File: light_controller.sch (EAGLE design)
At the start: 96 parts, among them IC1 ULN2803A, U1 DAC5578SPW, U2 LM3480IM3-5.0, U3 RCD-24-0.70

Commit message: updated all elements in schematic to be from openag_eagle_library repo
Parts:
- removed C12: 4.7uF, rcl:C-USC1206
- removed C13: 0.1uF, rcl:C-USC0603
- removed F6: (no value), fuse:GSH15
- removed IC1: ULN2803A, uln-udn:ULN2803A
- removed LED9: (no value), led:LED
- removed R17: 10k, rcl:R-US_R0603
- removed R18, R19, R20, R21, R25, R26, R27, R28: 0 ohm, rcl:R-US_R0603
- removed R24: 10 ohm, rcl:R-US_R0603
- removed R29, R30: 1K, rcl:R-US_R0603
- removed RELAY_1: G5LE-14_DC12, relay_2:G5LE-14_DC12
- removed S1: (no value), switch-omron:10-XX
- removed U$2: PHOTON_WITH_HEADERS, Spark:PHOTON_WITH_HEADERS
- removed U$4: SMAJ14A, openag_diodes:SMAJ14A
- added *CH7+, *CH7-: WIREPAD3,17/1,3, wirepad:WIREPAD3,17/1,3
- added C19, C20: 10uF, openag-capacitors:10UF-CL31B106KBHNNNE
- added D1: SMAJ14A, openag-diodes:SMAJ14A
- added F2, F3: SST 7, openag-fuses:SST_7
- added IC2: ULN2803A, openag-transistors:ULN2803DIP
- added LED2: (no value), openag-diodes:APT1608QBC/DCHIPLED_0603
- added R10, R13, R14, R15, R8, R9: 0 ohm, openag-resistors:0OHM-ERJ-3GEY0R00V
- added R3, R4: 10K, openag-resistors:10K-ERJ-3EKF1002V
- added R5, R6, R7: 1K, openag-resistors:1K-ERJ-PB3D1001V
- added TP26, TP27: PTR1B2,54, testpad:PTR1B2,54
- added U4: G5LE-14 DC24, openag-relays:G5LE-14_DC24
- added U5: ISO1540DR, openag-isolators:ISO1540DR
- C1: value 1uF -> 4.7uF; device rcl:C-USC0603 -> openag-capacitors:4.7UF-C1206C475K5PACTU
- C10, C3, C5: device rcl:C-USC1206 -> openag-capacitors:4.7UF-C1206C475K5PACTU
- C11, C8: value 10uF -> 0.1uF; device rcl:C-USC1206 -> openag-capacitors:0.1UF-C1206C104K5RAC7867
- C2, C6: device rcl:C-USC0603 -> openag-capacitors:0.1UF-C1206C104K5RAC7867
- C4: device rcl:C-USC1206 -> openag-capacitors:10UF-CL31B106KBHNNNE
- C7: value 10uF -> 1uF; device rcl:C-USC1206 -> openag-capacitors:1UF-CL10A105KB8NNNC
- C9: value 0.1uF -> 10uF; device rcl:C-USC0603 -> openag-capacitors:10UF-CL31B106KBHNNNE
- F1: value (none) -> SST 7; device fuse:GSH15 -> openag-fuses:SST_7
- L1: device openag-inductors:74404064121 -> openag-inductors:120UH-74404064121
- LED1: device led:LEDCHIP-LED0603 -> openag-diodes:APT1608QBC/DCHIPLED_0603
- R1: value 10K -> 10 ohm; device rcl:R-US_R0603 -> openag-resistors:10OHM-ERJ-3GEYJ100V
- R11, R12: value 1K -> 0 ohm; device rcl:R-US_R0603 -> openag-resistors:0OHM-ERJ-3GEY0R00V
- R2: value 0 ohm -> 1K; device rcl:R-US_R0603 -> openag-resistors:1K-ERJ-PB3D1001V
- TP1, TP2: device testpad:PTR1B2,54 -> openag-testpoints:PTR1B2,54
- U$1: value PSOC_4000 -> PHOTON_WITH_HEADERS; device stovelite:PSOC_4000 -> openag-microcontrollers:PHOTON_WITH_HEADERS
- U$3: value ISO1540 -> PSOC_4000; device ISO1540:ISO1540 -> openag-microcontrollers:PSOC_4000
- U2: device LEDdynamics:LM3480IM3-5.0 -> openag-regulators:LM3480IM3-5.0
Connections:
- removed net +12V: IC1.CD+, R24.1, RELAY_1.1, RELAY_1.2
- removed net 1C: IC1.O1, RELAY_1.5, TP1.TP
- removed net N$13: LED9.A, R17.1
- removed net N$4: IC1.I1, R2.2
- removed net P0: R17.2, R2.1
- removed net R1: F1.2, R1.2, TP2.TP
- new net CH7-: *CH7-.P, F1.2, R3.2, TP2.TP, TP27.TP
- new net DIM2: U1.VOUT_B
- new net DIM3: U1.VOUT_C
- new net DIM4: U1.VOUT_D
- new net DIM5: U1.VOUT_E
- new net DIM6: U1.VOUT_F
- new net N$5: F3.1, U3.+VOUT
- new net N$7: LED2.A, R4.1
- new net O1: IC2.18, TP1.TP, U4.5
- new net P6: U$3.P1.1
- new net P7: IC2.1, R4.2, U$3.P0.6
- net +24V: now also *CH7+.P, F2.2, IC2.10, R1.1, TP26.TP, U4.1, U4.2; no longer F6.2
- net +3V3: now also C1.1, C20.1, R2.2, R5.2, R8.2, U$3.VDD, U5.VCC2; no longer C3.1, C8.1, R18.2, R29.2, R30.2, S1.S1, U$1.VDD, U$3.VCC2
- net 24V_IN: now also C10.1, C9.1, D1.P$2, F2.1; no longer C12.1, C13.1, F6.1, U$4.P$2
- net CH1+: now also F3.2; no longer U3.+VOUT
- net GND1: now also C19.2, U5.GND1; no longer C7.2, U$3.GND1
- net GND2: now also C20.2, C7.2, D1.P$1, IC2.9, LED2.C, U$1.GND@2, U$1.GND@21, U$3.VSS, U5.GND2; no longer C12.2, C13.2, IC1.GND, LED9.C, U$1.VSS, U$2.GND@2, U$2.GND@21, U$3.GND2, U$4.P$1
- net I2C_3V3: now also C19.1, R6.2, R7.2, U5.VCC1; no longer C7.1, R11.2, R12.2, U$3.VCC1
- net I2C_SCL: now also R6.1, R7.1, U5.SCL1; no longer R12.1, U$3.SCL1
- net I2C_SDA: now also U5.SDA1; no longer R11.1, U$3.SDA1
- net N$1: now also R3.1; no longer R1.1
- net N$2: now also U4.3; no longer RELAY_1.3
- net N$21: now also R13.1, U$1.D2; no longer R26.1, U$2.D2
- net N$22: now also R14.1, U$1.D1; no longer R27.1, U$2.D1
- net N$23: now also C3.1, C8.1, R8.1, U$1.3V3; no longer C10.1, C9.1, R18.1, U$2.3V3
- net N$24: now also R9.1, U$1.D6; no longer R19.1, U$2.D6
- net N$25: now also R10.1, U$1.D5; no longer R20.1, U$2.D5
- net N$26: now also R11.1, U$1.D4; no longer R21.1, U$2.D4
- net N$27: now also R12.1, U$1.D3; no longer R25.1, U$2.D3
- net N$28: now also R15.1, U$1.D0; no longer R28.1, U$2.D0
- net N$29: now also C7.1, U$3.VCCD; no longer C1.1, U$1.VCCD
- net N$39: now also R1.2; no longer R24.2
- net P1: now also R9.2, U$3.P2.0; no longer R19.2, S1.P1, U$1.P2.0
- net P2: now also R10.2, U$3.P1.7; no longer R20.2, U$1.P1.7
- net P3: now also R11.2, U$3.P1.6; no longer R21.2, U$1.P1.6
- net P4: now also R12.2, U$3.P1.3; no longer R25.2, U$1.P1.3
- net P5: now also R13.2, U$3.P1.2; no longer R26.2, U$1.P1.2
- net SCL: now also R14.2, R5.1, U$3.P3.1, U5.SCL2; no longer R27.2, R30.1, U$1.P3.1, U$3.SCL2
- net SDA: now also R15.2, R2.1, U$3.P3.0, U5.SDA2; no longer R28.2, R29.1, U$1.P3.0, U$3.SDA2
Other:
- note added: "Current Regulators Module"
- note added: "Multi-Channel DAC Module"
- note added: "TODO: Same circuit for channels 2-6"
- note removed: "LM3480IM3-5.0"
- note removed: "Pushbutton Switch Module"
- moved on the sheet: C14, C15, C16, C17, C18, C9, L1, LED1, TP1, TP2, U1, U3

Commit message: calculated power consuption, cleaned up mcu 0ohnm resistors
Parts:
- removed *CH7+, *CH7-: WIREPAD3,17/1,3, wirepad:WIREPAD3,17/1,3
- removed C4: 10uF, openag-capacitors:10UF-CL31B106KBHNNNE
- removed C5: 4.7uF, openag-capacitors:4.7UF-C1206C475K5PACTU
- removed C6: 0.1uF, openag-capacitors:0.1UF-C1206C104K5RAC7867
- removed F1: SST 7, openag-fuses:SST_7
- removed IC2: ULN2803A, openag-transistors:ULN2803DIP
- removed LED1, LED2: (no value), openag-diodes:APT1608QBC/DCHIPLED_0603
- removed R1: 10 ohm, openag-resistors:10OHM-ERJ-3GEYJ100V
- removed TP1, TP2: PTR1B2,54, openag-testpoints:PTR1B2,54
- removed TP11, TP26, TP27: PTR1B2,54, testpad:PTR1B2,54
- removed U2: LM3480IM3-5.0, openag-regulators:LM3480IM3-5.0
- removed U4: G5LE-14 DC24, openag-relays:G5LE-14_DC24
- added R16, R17, R18, R20, R21, R22, R23, R24, R25, R26, R27, R28, R29, R30, R31, R32, R33: 0 ohm, openag-resistors:0OHM-ERJ-3GEY0R00V
- C1: value 4.7uF -> 1uF; device openag-capacitors:4.7UF-C1206C475K5PACTU -> openag-capacitors:1UF-CL10A105KB8NNNC
- C7: value 1uF -> 0.1uF; device openag-capacitors:1UF-CL10A105KB8NNNC -> openag-capacitors:0.1UF-C1206C104K5RAC7867
- R3, R4: value 10K -> 0 ohm; device openag-resistors:10K-ERJ-3EKF1002V -> openag-resistors:0OHM-ERJ-3GEY0R00V
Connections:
- removed net CH7-: *CH7-.P, F1.2, R3.2, TP2.TP, TP27.TP
- removed net N$39: C4.1, R1.2, U2.IN
- removed net O1: IC2.18, TP1.TP, U4.5
- new net N$10: R21.1, U$3.P1.7
- new net N$11: R22.1, U$3.P1.6
- new net N$12: R23.1, U$3.P1.3
- new net N$13: R24.1, U$3.P1.2
- new net N$14: R25.1, U$3.P1.1
- new net N$15: C7.2, R26.2
- new net N$16: C1.1, C2.1, R27.1, U$3.VDD
- new net N$17: C1.2, C2.2, R28.2
- new net N$18: R29.2, U$3.VSS
- new net N$19: R30.2, U$1.GND@2
- new net N$20: C3.2, C8.2, R31.2
- new net N$30: R32.1, U$1.GND@21
- new net N$31: R33.1, U$3.P0.6
- new net N$4: R16.1, U$1.A5
- new net N$6: R17.1, U$1.A4
- new net N$8: R18.2, U1.!CLR!
- net +24V: no longer *CH7+.P, IC2.10, R1.1, TP26.TP, U4.1, U4.2
- net +3V3: now also R27.2; no longer C1.1, C2.1, C5.1, C6.1, TP11.TP, U$3.VDD, U2.OUT
- net GND2: now also R26.1, R28.1, R29.1, R30.1, R31.1, R32.2; no longer C1.2, C2.2, C3.2, C4.2, C5.2, C6.2, C7.2, C8.2, IC2.9, LED1.C, LED2.C, U$1.GND@2, U$1.GND@21, U$3.VSS, U2.GND
- net N$1: now also R3.2, U$3.P3.0; no longer LED1.A, R3.1
- net N$2: now also R4.2, U$3.P3.1; no longer F1.1, U4.3
- net N$7: now also R20.1, U$3.P2.0; no longer LED2.A, R4.1
- net P1: now also R20.2; no longer U$3.P2.0
- net P2: now also R21.2; no longer U$3.P1.7
- net P3: now also R22.2; no longer U$3.P1.6
- net P4: now also R23.2; no longer U$3.P1.3
- net P5: now also R24.2; no longer U$3.P1.2
- net P6: now also R16.2, R25.2; no longer U$3.P1.1
- net P7: now also R17.2, R18.1, R33.2; no longer IC2.1, R4.2, U$3.P0.6
- net SCL: now also R4.1; no longer U$3.P3.1
- net SDA: now also R3.1; no longer U$3.P3.0
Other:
- note removed: "3V3 Regulator Module"
- note removed: "Relay Driver Module"
- note removed: "Relay Module"
- moved on the sheet: +24V, C1, C10, C11, C14, C15, C16, C17, C18, C19, C2, C20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

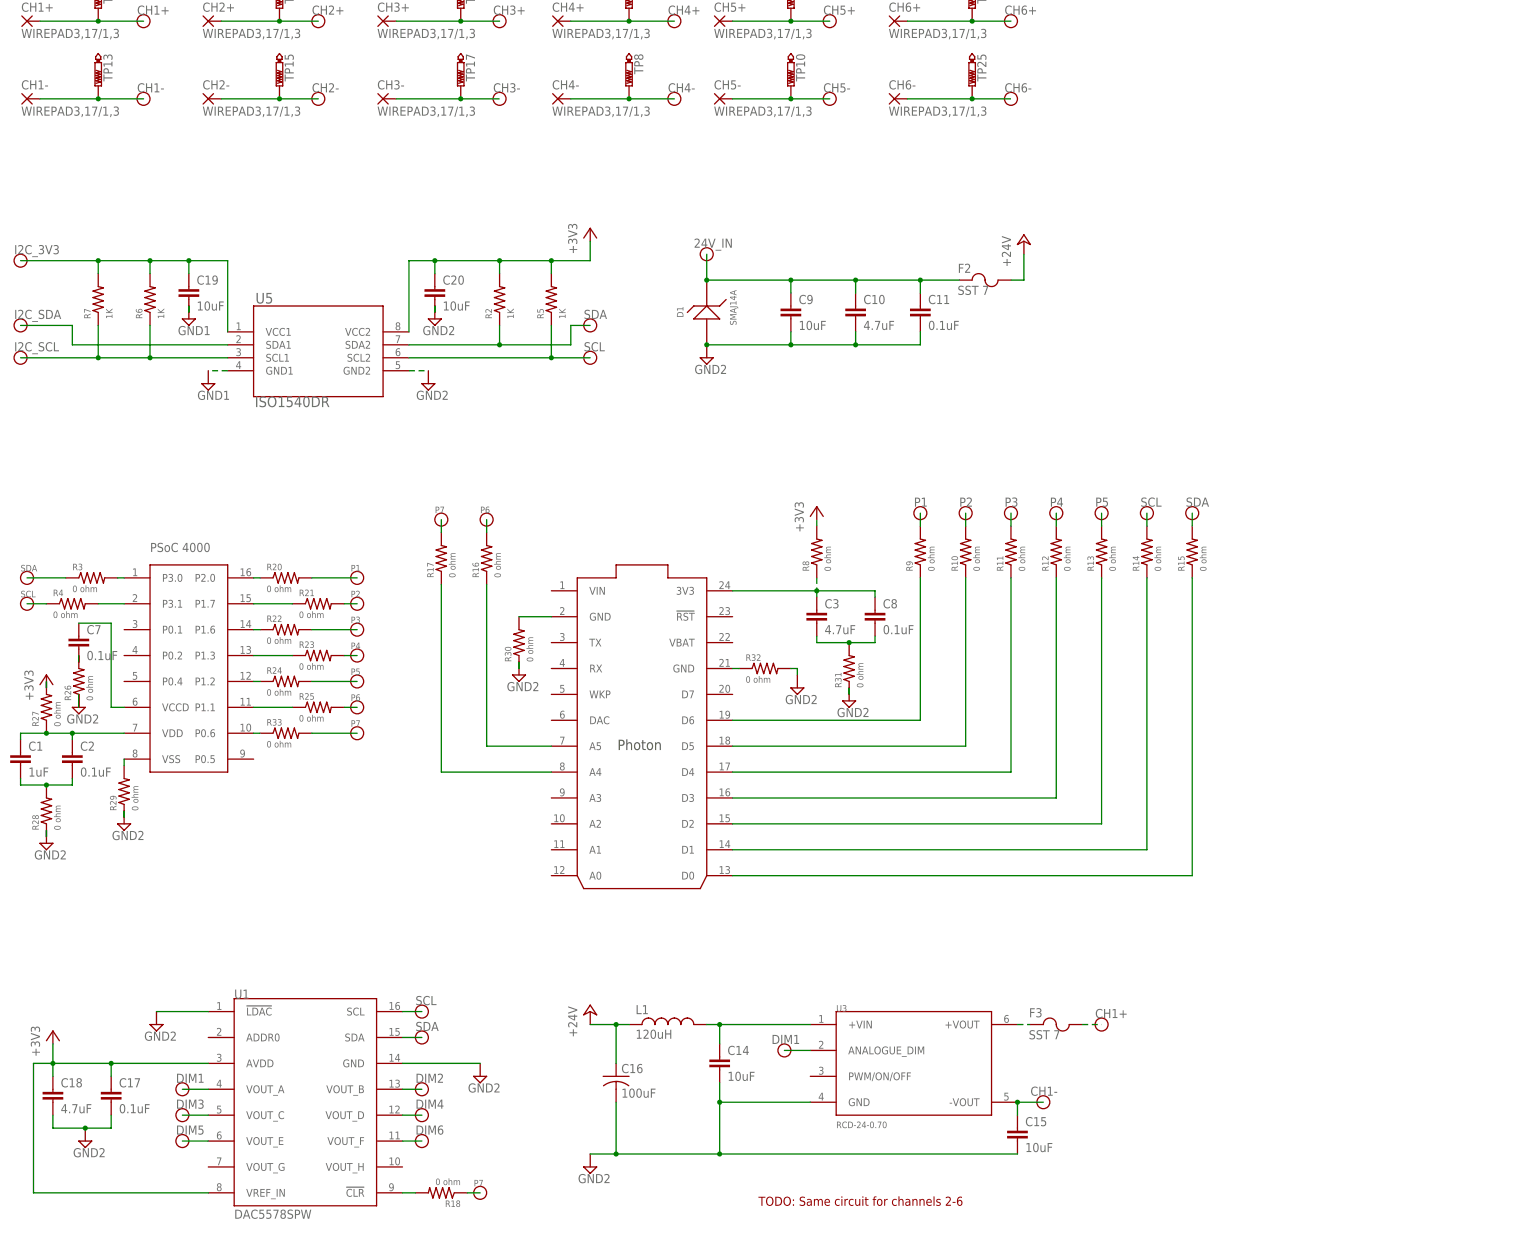
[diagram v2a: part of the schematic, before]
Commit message: added 3v3 syncronous regulator module
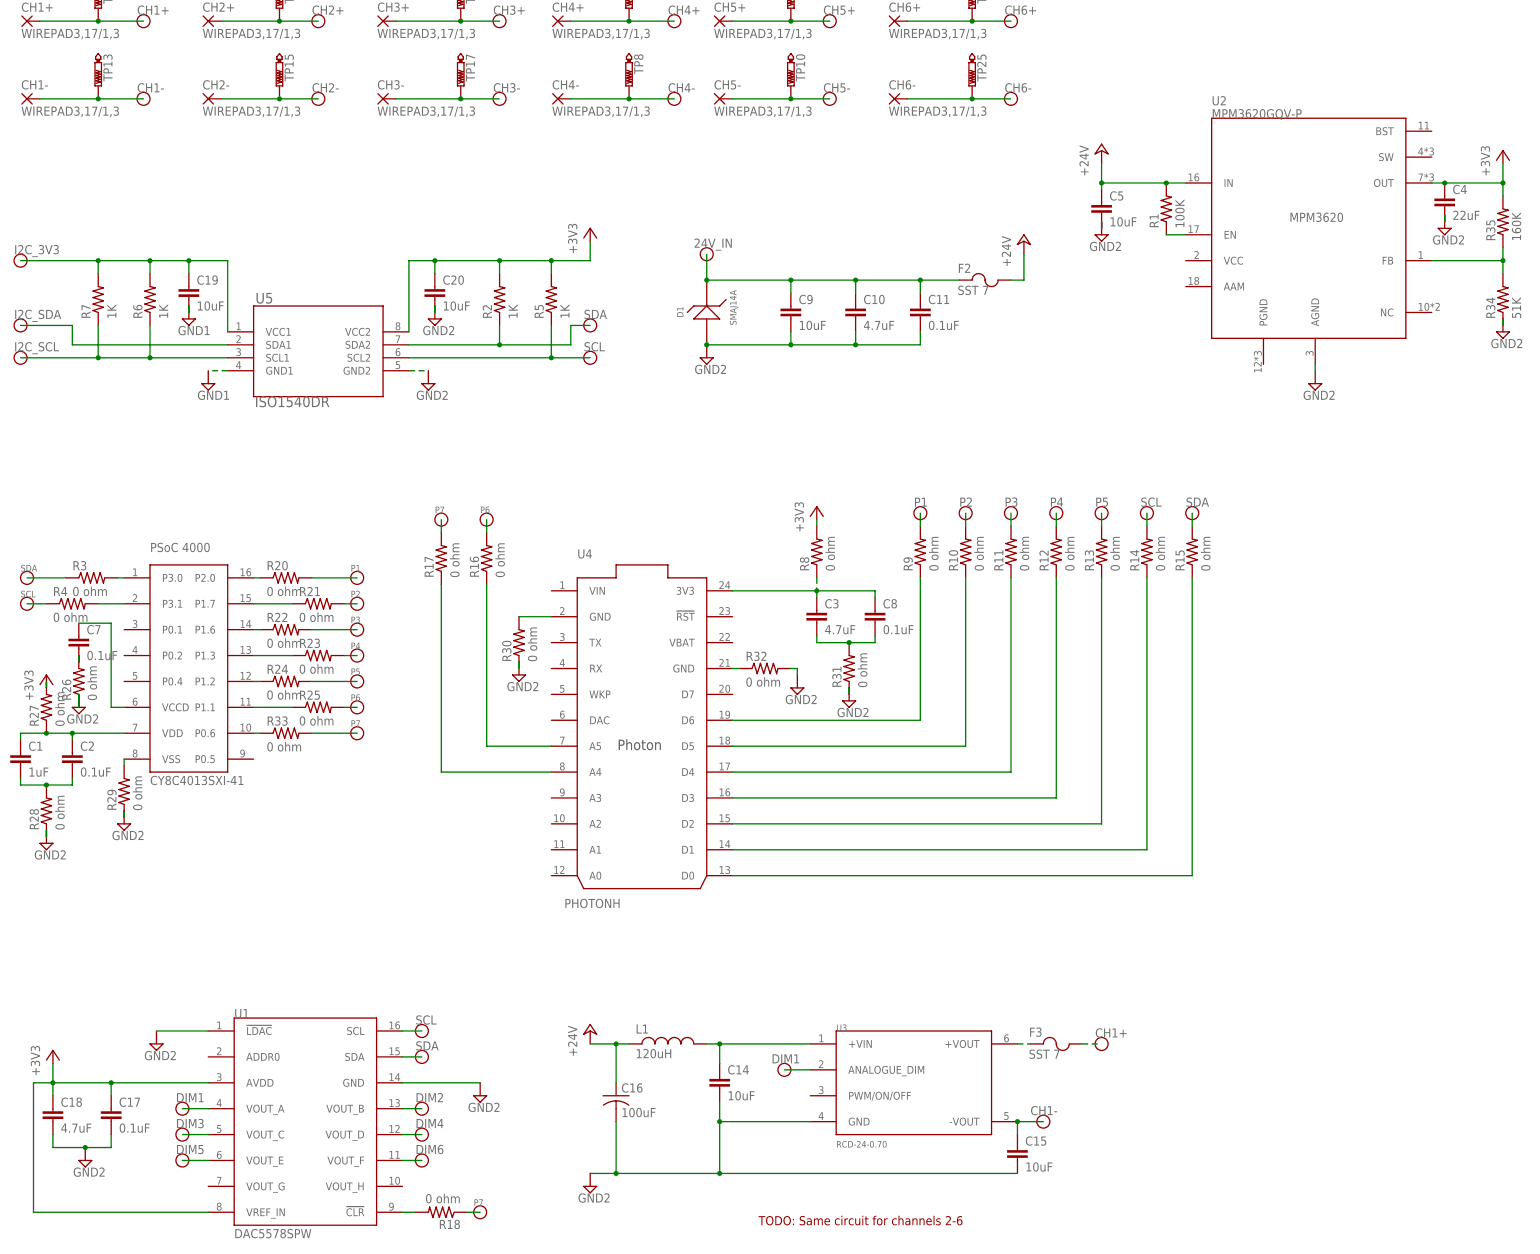
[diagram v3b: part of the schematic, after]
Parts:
- removed U$1: PHOTON_WITH_HEADERS, openag-microcontrollers:PHOTON_WITH_HEADERS
- removed U$3: PSOC_4000, openag-microcontrollers:PSOC_4000
- added C4: 22uF, openag-capacitors:22UF-C3216X5R1V226M160AC
- added C5: 10uF, openag-capacitors:10UF-CL31B106KBHNNNE
- added R1: 100K, openag-resistors:100K-RC0603FR-07100KL
- added R34: 51K, openag-resistors:51K-RC0603JR-0751KL
- added R35: 160K, openag-resistors:160K-RC0603JR-07160KL
- added U$2: CY8C4013SXI-41, openag-microcontrollers:CY8C4013SXI-41
- added U2: MPM3620GQV-P, openag-regulators:MPM3620GQV-P
- added U4: PHOTONH, openag-microcontrollers:PHOTONHPHOTONH
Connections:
- new net N$32: R1.1, U2.EN
- new net N$33: R34.2, R35.1, U2.FB
- net +24V: now also C5.1, R1.2, U2.IN
- net +3V3: now also C4.1, R35.2, U2.OUT
- net GND2: now also C4.2, C5.2, R34.1, U2.AGND
- net N$1: now also U$2.P3.0; no longer U$3.P3.0
- net N$10: now also U$2.P1.7; no longer U$3.P1.7
- net N$11: now also U$2.P1.6; no longer U$3.P1.6
- net N$12: now also U$2.P1.3; no longer U$3.P1.3
- net N$13: now also U$2.P1.2; no longer U$3.P1.2
- net N$14: now also U$2.P1.1; no longer U$3.P1.1
- net N$16: now also U$2.VDD; no longer U$3.VDD
- net N$18: now also U$2.VSS; no longer U$3.VSS
- net N$19: now also U4.GND@2; no longer U$1.GND@2
- net N$2: now also U$2.P3.1; no longer U$3.P3.1
- net N$21: now also U4.D2; no longer U$1.D2
- net N$22: now also U4.D1; no longer U$1.D1
- net N$23: now also U4.3V3; no longer U$1.3V3
- net N$24: now also U4.D6; no longer U$1.D6
- net N$25: now also U4.D5; no longer U$1.D5
- net N$26: now also U4.D4; no longer U$1.D4
- net N$27: now also U4.D3; no longer U$1.D3
- net N$28: now also U4.D0; no longer U$1.D0
- net N$29: now also U$2.VCCD; no longer U$3.VCCD
- net N$30: now also U4.GND@21; no longer U$1.GND@21
- net N$31: now also U$2.P0.6; no longer U$3.P0.6
- net N$4: now also U4.A5; no longer U$1.A5
- net N$6: now also U4.A4; no longer U$1.A4
- net N$7: now also U$2.P2.0; no longer U$3.P2.0
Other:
- note added: "3v3 Synchronous Regulator Module"
- moved on the sheet: C14, C15, C16, C17, C18, F3, L1, R18, U1, U3
